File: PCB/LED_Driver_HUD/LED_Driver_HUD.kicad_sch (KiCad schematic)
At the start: 7 parts, among them J1 Conn_02x05_Odd_Even, U1 TLC5947DAP, U2 TLC5947DAP

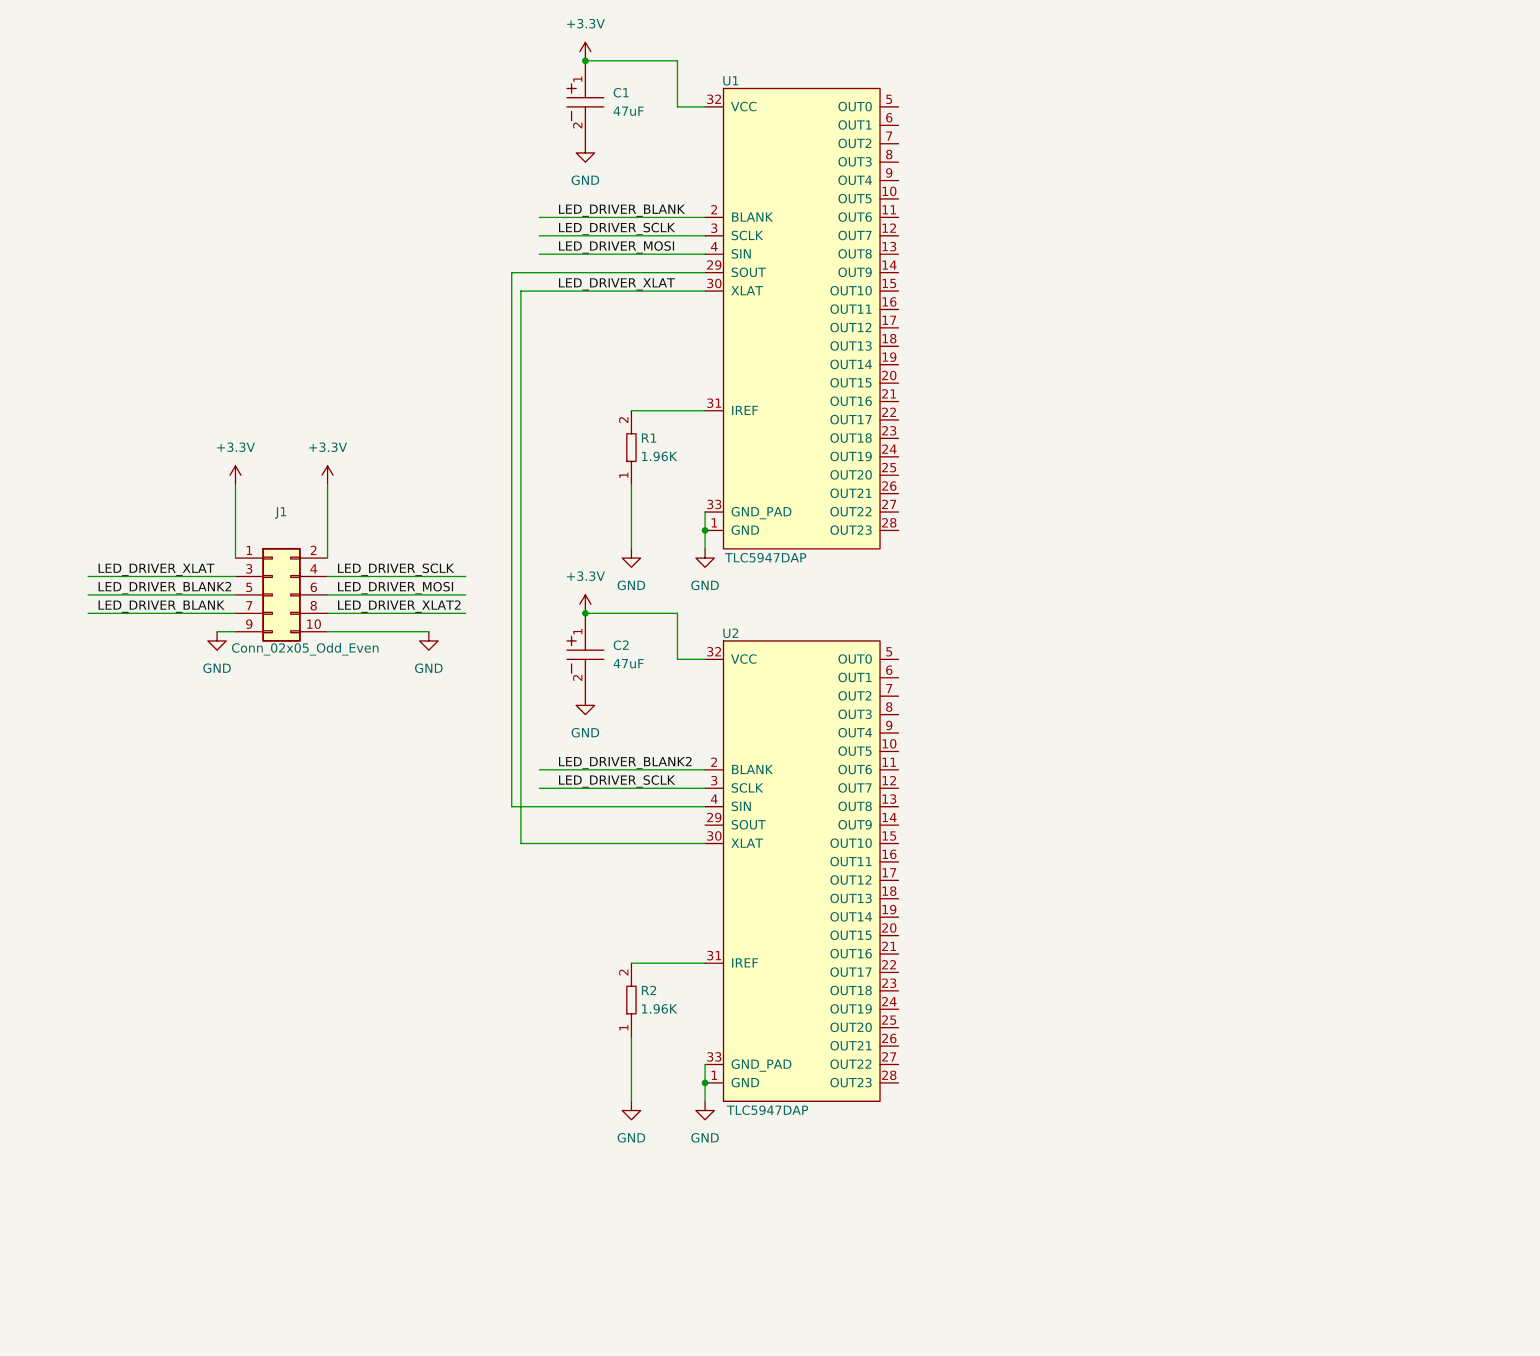
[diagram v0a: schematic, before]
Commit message: RJ45
Replaced RJ45 connector, original one had magnetics, those are not needed for RS485 and would have caused problems. Hooked up coms LEDs on RJ45 connector to MCU for debugging and displaying coms activity.
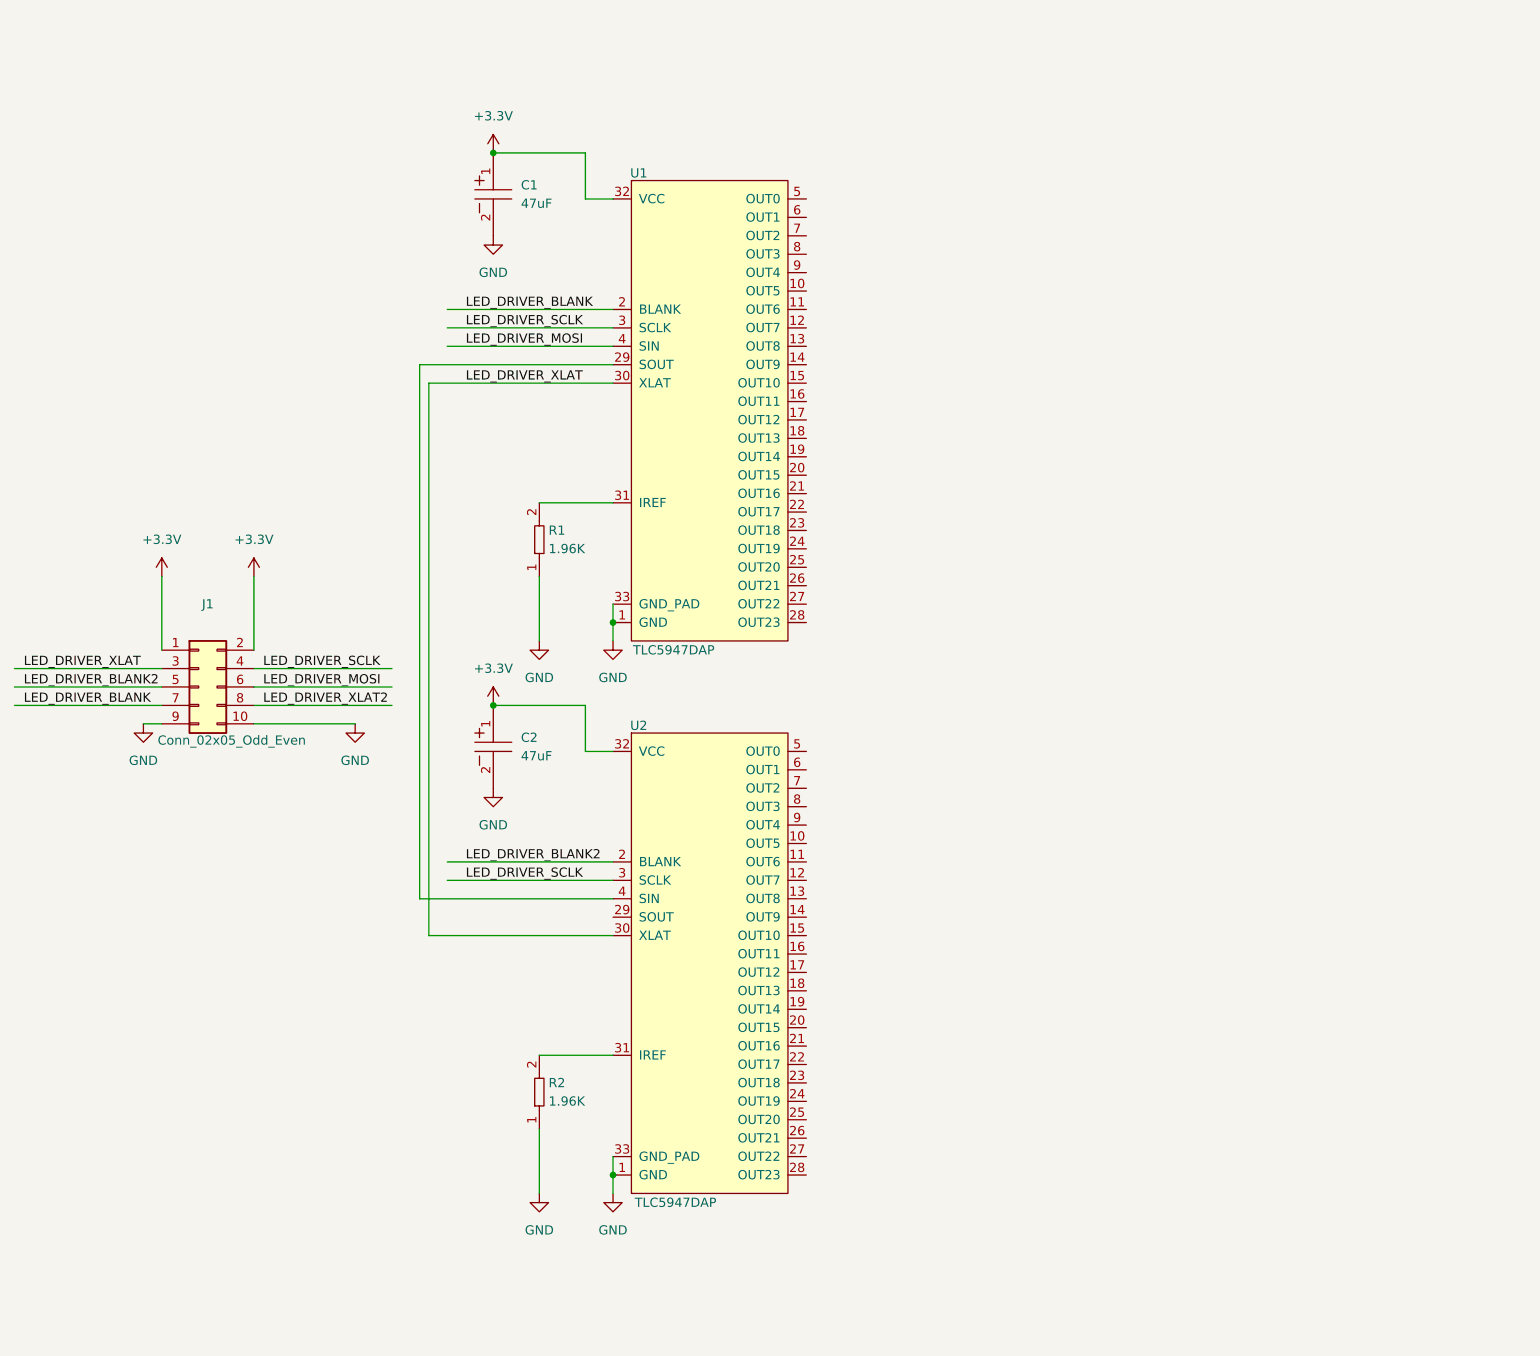
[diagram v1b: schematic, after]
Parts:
- J1: footprint (none) -> Connector_PinHeader_2.54mm:PinHeader_2x05_P2.54mm_Vertical
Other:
- moved on the sheet: C1, C2, J1, R1, R2, U1, U2

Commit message: LED Driver HUD
Finished PCB design of LED Driver HUD PCB, First pass of route DRC full pass. Next update adding additional LEDs for additional display functions
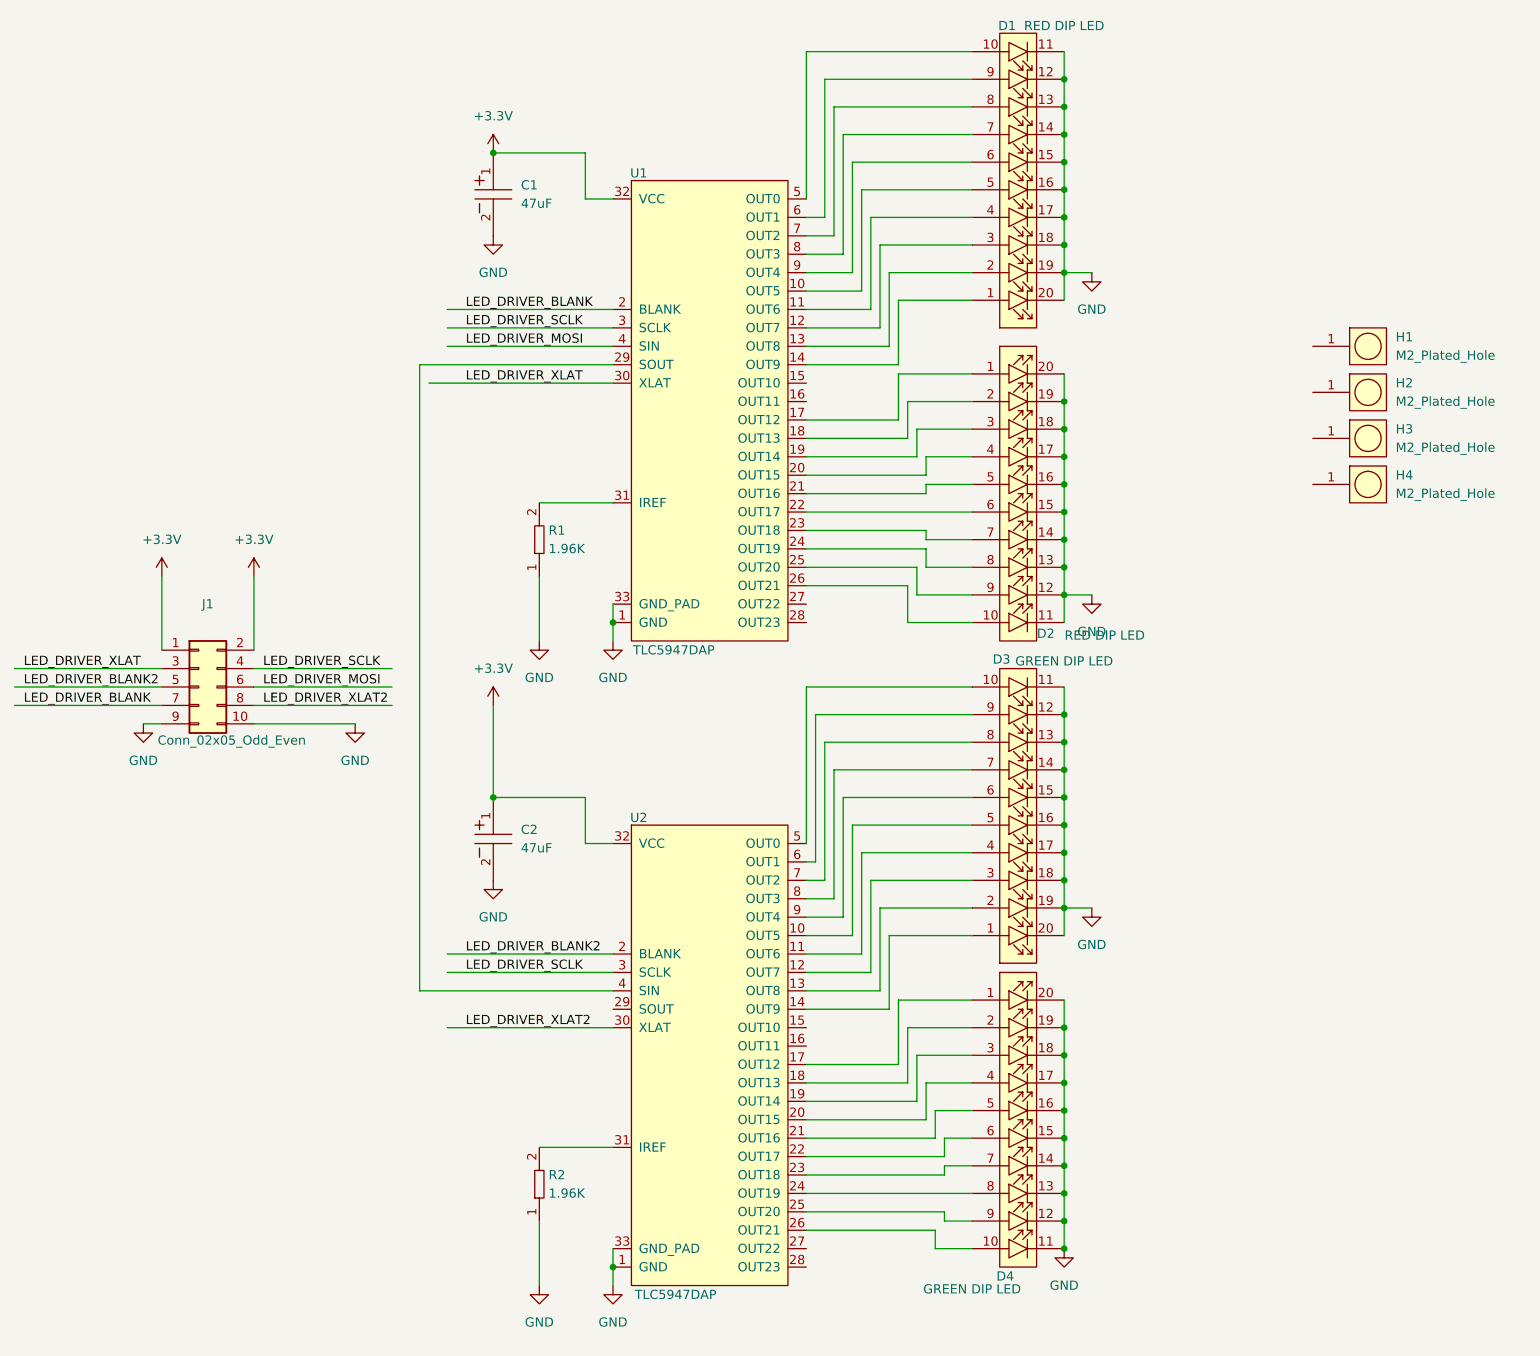
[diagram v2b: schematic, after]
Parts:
- added D1, D2: DC10EWA, AVR-KiCAD-Lib-Diodes:DIP750W50P254L2540H825Q20, symbol AVR-KiCAD-Lib-Diodes:DC10EWA
- added D3, D4: DC10GWA, AVR-KiCAD-Lib-Diodes:DIP750W50P254L2540H825Q20, symbol AVR-KiCAD-Lib-Diodes:DC10GWA
- added H1, H2, H3, H4: M2_Plated_Hole, AVR-KiCAD-Lib-Holes_Fasteners:M2_HOLE, symbol AVR-KiCAD-Lib-Holes_Fasteners:M2_Plated_Hole
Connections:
- net GND: now also D1.11, D1.12, D1.13, D1.14, D1.15, D1.16, D1.17, D1.18, D1.19, D1.20, D2.11, D2.12, D2.13, D2.14, D2.15, D2.16, D2.17, D2.18, D2.19, D2.20, D3.11, D3.12, D3.13, D3.14, D3.15, D3.16, D3.17, D3.18, D3.19, D3.20, D4.11, D4.12, D4.13, D4.14, D4.15, D4.16, D4.17, D4.18, D4.19, D4.20
- net LED_DRIVER_XLAT: no longer U2.30 (XLAT)
- net LED_DRIVER_XLAT2: now also U2.30 (XLAT)
- net at U1.10 (OUT5): now also D1.5
- net at U1.11 (OUT6): now also D1.4
- net at U1.12 (OUT7): now also D1.3
- net at U1.13 (OUT8): now also D1.2
- net at U1.14 (OUT9): now also D1.1
- net at U1.17 (OUT12): now also D2.1
- net at U1.18 (OUT13): now also D2.2
- net at U1.19 (OUT14): now also D2.3
- net at U1.20 (OUT15): now also D2.4
- net at U1.21 (OUT16): now also D2.5
- net at U1.22 (OUT17): now also D2.6
- net at U1.23 (OUT18): now also D2.7
- net at U1.24 (OUT19): now also D2.8
- net at U1.25 (OUT20): now also D2.9
- net at U1.26 (OUT21): now also D2.10
- net at U1.5 (OUT0): now also D1.10
- net at U1.6 (OUT1): now also D1.9
- net at U1.7 (OUT2): now also D1.8
- net at U1.8 (OUT3): now also D1.7
- net at U1.9 (OUT4): now also D1.6
- net at U2.10 (OUT5): now also D3.5
- net at U2.11 (OUT6): now also D3.4
- net at U2.12 (OUT7): now also D3.3
- net at U2.13 (OUT8): now also D3.2
- net at U2.14 (OUT9): now also D3.1
- net at U2.17 (OUT12): now also D4.1
- net at U2.18 (OUT13): now also D4.2
- net at U2.19 (OUT14): now also D4.3
- net at U2.20 (OUT15): now also D4.4
- net at U2.21 (OUT16): now also D4.5
- net at U2.22 (OUT17): now also D4.6
- net at U2.23 (OUT18): now also D4.7
- net at U2.24 (OUT19): now also D4.8
- net at U2.25 (OUT20): now also D4.9
- net at U2.26 (OUT21): now also D4.10
- net at U2.5 (OUT0): now also D3.10
- net at U2.6 (OUT1): now also D3.9
- net at U2.7 (OUT2): now also D3.8
- net at U2.8 (OUT3): now also D3.7
- net at U2.9 (OUT4): now also D3.6
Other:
- moved on the sheet: C2, R2, U2

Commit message: LED HUD Complete
Added Additional indicator LEDs to LED HUD board. Full DRC pass.
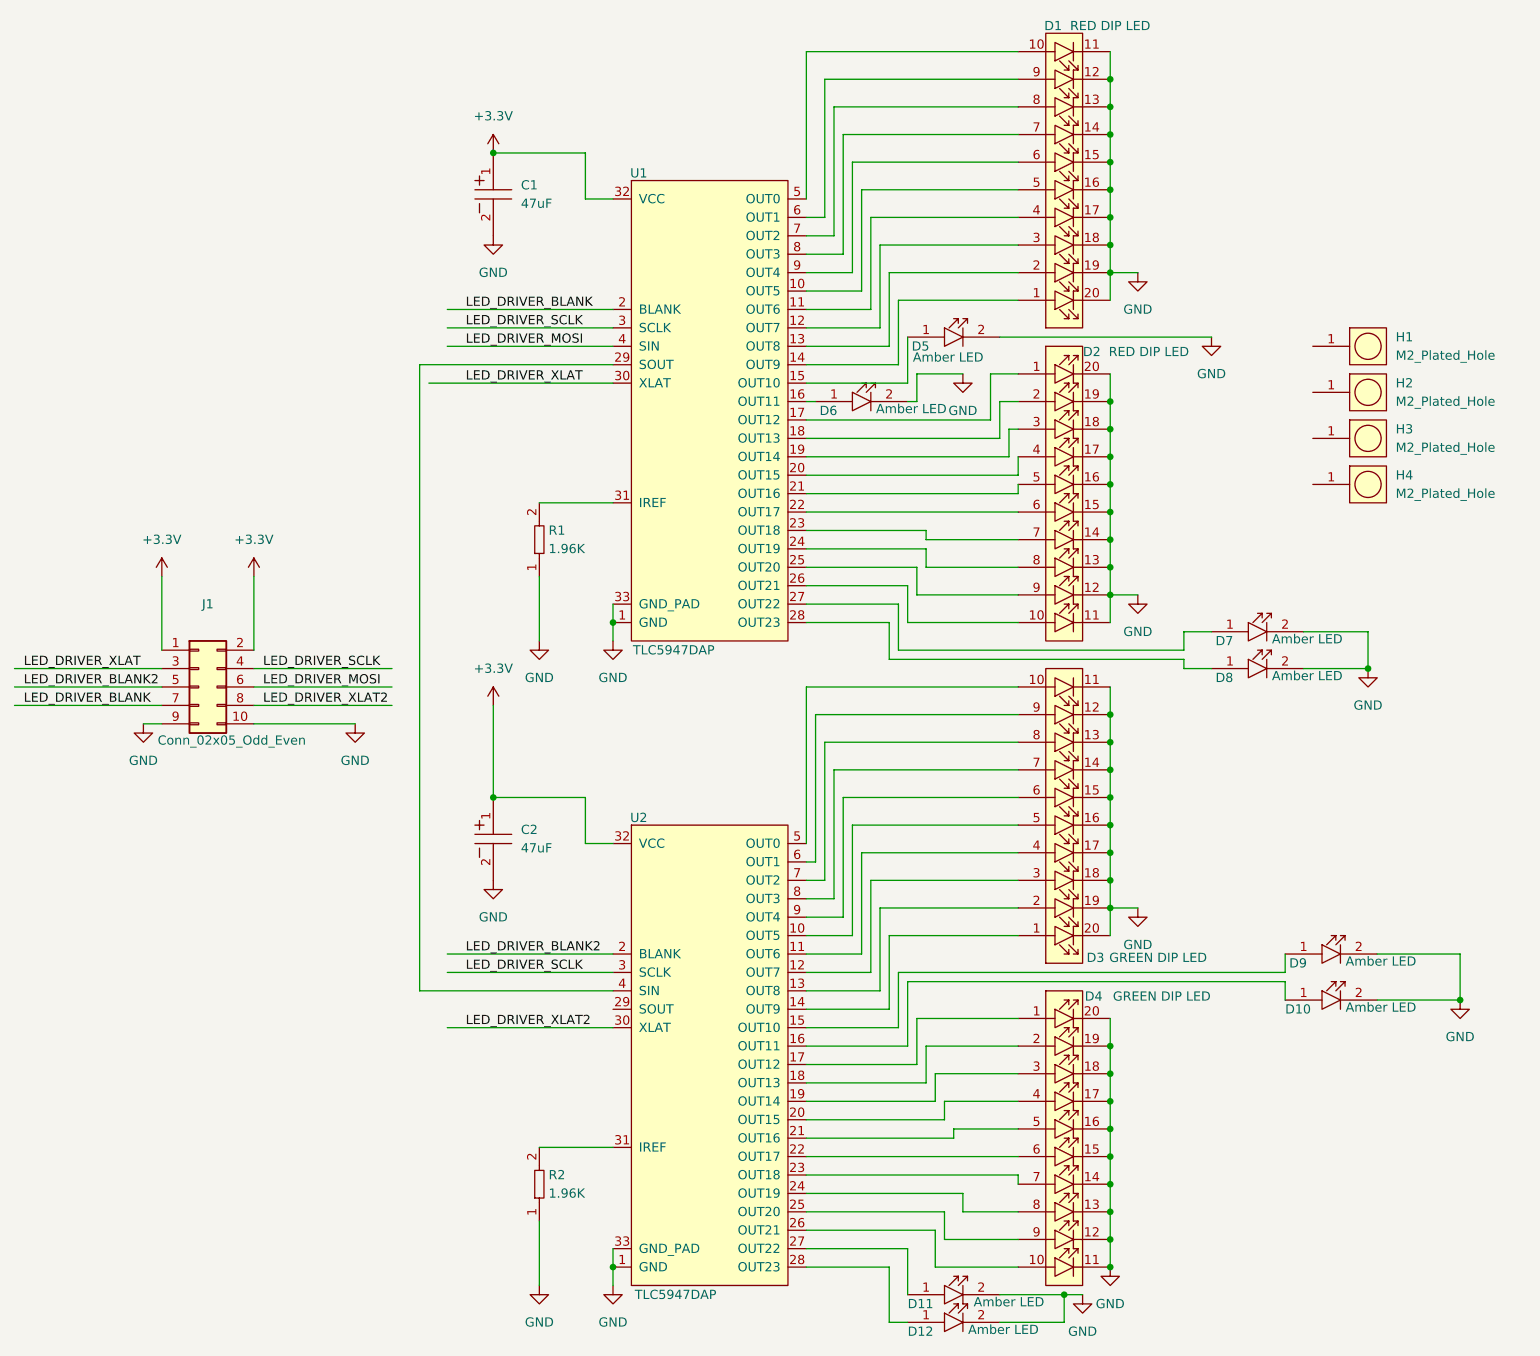
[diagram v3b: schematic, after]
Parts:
- added D10, D11, D12, D5, D6, D7, D8, D9: HLMP-1401, AVR-KiCAD-Lib-Diodes:HLMP, symbol AVR-KiCAD-Lib-Diodes:HLMP-1401
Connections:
- net GND: now also D10.2, D11.2, D12.2, D5.2, D6.2, D7.2, D8.2, D9.2
- net at U1.15 (OUT10): now also D5.1
- net at U1.16 (OUT11): now also D6.1
- net at U1.27 (OUT22): now also D7.1
- net at U1.28 (OUT23): now also D8.1
- net at U2.15 (OUT10): now also D9.1
- net at U2.16 (OUT11): now also D10.1
- net at U2.27 (OUT22): now also D11.1
- net at U2.28 (OUT23): now also D12.1
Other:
- moved on the sheet: D1, D2, D3, D4
